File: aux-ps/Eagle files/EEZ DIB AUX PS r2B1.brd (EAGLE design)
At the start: 210 x 60 mm, 117 parts, among them IC1 AMC6821SDBQR, IC2 VIPer35L, IC3 TL431, J1 PF0030/PC, J2 1-726388-2, J3 1-726388-2, J4 1-726388-2, J5 SWEB 8094 AU/GN, Q1 BTA26-600, Q2 BTA26-600, Q3 2N7002, Q4 2N7002, Q5 BSP716NH6327XTSA1, Q6 2N7002, SW1 DF62J12S2AHQA, X1 39-28-1063, X2 39-30-1039, X3 ZL231-16KG, X4 22-23-2031, X5 22-23-2021

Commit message: #30, #31, #32
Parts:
- removed D7: BAS316, EEZ_Lib1:SOD323-R
- removed L4: ECS-MPIL0630-150MC, EEZ_inductors_and_transformers:DE0704
- removed TR1B: (WE 760875532), EEZ_Lib1:WE-UOST
- added C25: 18p, rcl:C0603
- added C26: 33n, rcl:C0805
- added C27: 2n2, rcl:C0805
- added R38: 10K, rcl:R0805
- added R39: 6K8, rcl:R0805
- added R40: 47K, rcl:R0805
- added R41: 4K7, rcl:R0805
- added X6: 22-23-2021, con-molex:22-23-2021
- added ZD4: N.C., EEZ_Lib1:SOD123
- added ZD5: BZT52C20-DC, EEZ_Lib1:SOD123
- C10: value 3n3 -> 1n/1kV; device rcl:C0805 -> rcl:C1210
- C11: value 3n3 -> UCY2G6R8MPD; device rcl:C0805 -> EEZ_Lib1:ECAP5/10.5
- C12: value UVZ1C471MPD -> UCY2G6R8MPD; device EEZ_Lib1:ECAP3.5/8 -> EEZ_Lib1:ECAP5/10.5
- C13: value 4u7 -> 3n3; device rcl:C1210 -> rcl:C0805
- C14: value EEEFK1V470P -> UVZ1C471MPD; device EEZ_Lib1:CAPAE660X610N -> EEZ_Lib1:ECAP3.5/8
- C15: value CY1Y-470P -> 4u7; device EEZ_Lib1:CY075-032X103 -> rcl:C1210
- C16: value 100n -> 3n3; device rcl:C0603 -> rcl:C0805
- C17: value 3n3 -> EEEFK1V470P; device rcl:C0805 -> EEZ_Lib1:CAPAE660X610N
- C18: value 1500u/16V -> CY1Y-470P; device EEZ_Lib1:ECAP5/13 -> EEZ_Lib1:CY075-032X103
- C19: value 4u7 -> 100n; device rcl:C1210 -> rcl:C0603
- C20: value N.C. -> 3n3
- C21: value 33n -> 1500u/16V; device rcl:C0805 -> EEZ_Lib1:ECAP5/13
- C22: value 18p -> 4u7; device rcl:C0603 -> rcl:C1210
- C23: value 33n -> N.C.
- C24: value 2n2 -> 33n
- C4: value 10u -> 1u; device rcl:C1206 -> rcl:C0805
- C5: value UVZ1C471MPD -> 1u; device EEZ_Lib1:ECAP3.5/8 -> rcl:C0805
- C7: value 1n/1kV -> 100n; device rcl:C1210 -> rcl:C0805
- C8, C9: value UCY2G6R8MPD -> 100n; device EEZ_Lib1:ECAP5/10.5 -> rcl:C0603
- D1: value SKL16 -> SS110; device EEZ_Lib1:SOD123 -> EEZ_Lib1:SMB
- D2: value SS110 -> US1K-DIO; device EEZ_Lib1:SMB -> EEZ_Lib1:DO214AA
- D3: value US1K-DIO -> SS110; device EEZ_Lib1:DO214AA -> EEZ_Lib1:SMB
- D4: value SS110 -> SK55
- D5: value SK55 -> BAS316; device EEZ_Lib1:SMB -> EEZ_Lib1:SOD323-R
- IC1: value AMC6821SDBQR -> MAX31760AEE+
- L1: value BLM21PG331SH1 -> RLB0812-471KL; device EEZ_Lib1:0805 -> EEZ_Lib1:FERSYTER_DSZ6
- L2: value RLB0812-471KL -> ECS-MPIL0630-150MC; device EEZ_Lib1:FERSYTER_DSZ6 -> EEZ_inductors_and_transformers:DE0704
- L3: value DLG-0403-180 -> ECS-MPIL0630-150MC; device EEZ_inductors_and_transformers:DE0403 -> EEZ_inductors_and_transformers:DE0704
- Q5: value BSP716NH6327XTSA1 -> 2N7002; device transistor-power:SOT223 -> EEZ_Lib1:SOT103P240X110-3N
- Q6: value 2N7002 -> PSMN0R9-25YLC; device EEZ_Lib1:SOT103P240X110-3N -> EEZ_Lib1:SOT669
- R11: value 2K2 -> 1R
- R12: value 10K -> 470R
- R13: value 470R -> 1K
- R14: value 47K -> 1K
- R15: value 10K -> 4K7
- R16: value 4K7 -> 47K
- R17: value 2K2 -> 10R
- R18: value 220K -> 100R; device rcl:R1206 -> rcl:R0805
- R19: value 220K -> N.C.; device rcl:R1206 -> rcl:R0805
- R20: value 100K -> 10R; device rcl:R1206 -> rcl:R0805
- R21, R22: value 120R -> 100K; device rcl:R0805 -> rcl:R1206
- R23, R28: value 1K -> 100K; device rcl:R0805 -> rcl:R1206
- R24: value 100K -> 120R; device rcl:R1206 -> rcl:R0805
- R25: value 22R -> 100K; device rcl:R0805 -> rcl:R1206
- R26: value 100K -> 1K; device rcl:R1206 -> rcl:R0805
- R27: value 120R -> 22R
- R29: value N.C. -> 120R
- R30: value 4K87 -> 120R
- R31: value 10K -> 1K
- R32: value 47K -> 4K7
- R33: value 10K -> N.C.
- R34: value 6K8 -> 10K
- R35: value 1K8 -> 47K
- R36: value 47K -> 270R
- R37: value 4K7 -> 1K8
- X4: value 22-23-2031 -> 47053-1000; device con-molex:22-23-2031 -> EEZ_connectors:47053-1000
- X5: value 22-23-2021 -> 47053-1000; device con-molex:22-23-2021 -> EEZ_connectors:47053-1000
- ZD3: value BZT52C20-DC -> N.C.
- moved C12 79.4 mm to (134.6, 29.9)
- moved C19 79.0 mm to (129.7, 35.2), turned to 90 degrees
- moved C17 78.2 mm to (135.7, 51.8)
- moved R33 73.3 mm to (135.6, 40.1), turned to 180 degrees
- moved D5 72.0 mm to (136.0, 43.3), turned to 90 degrees
- moved R36 71.3 mm to (51.6, 18.0)
- moved R32 70.7 mm to (51.6, 22.0), turned to 90 degrees
- moved R37 70.2 mm to (129.5, 43.4), turned to 90 degrees
- moved C9 69.2 mm to (51.1, 41.8)
- moved R27 68.7 mm to (125.2, 56.3), turned to 0 degrees
- moved X5 64.1 mm to (103.1, 55.4)
- moved R19 64.1 mm to (45.3, 42.2)
- moved ZD3 63.8 mm to (53.1, 41.5)
- moved C22 62.3 mm to (58.4, 27.1), turned to 0 degrees
- moved R21 61.0 mm to (121.5, 23.0)
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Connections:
- removed net +12V_FAN: C3.1, C5.+, D1.C, L1.1, R12.2, X4.1
- removed net FAN_SENSE: R12.1, R15.2, X4.3
- removed net N$58: IC1.1, Q5.1, R11.2
- new net DRAIN: C7.1, Q6.MB, R11.1
- new net FAN_SENSE1: R13.1, R17.2, X4.3, ZD4.C
- new net FAN_SENSE2: R14.1, R20.2, X5.3, ZD3.C
- new net N$15: C7.2, Q6.4, R18.2
- new net N$17: R21.2, R23.2
- new net N$21: C9.1, IC1.9, R20.1
- new net N$22: R32.1, R36.2
- new net PWM_OUT: IC1.6, R15.2, R18.1, X4.4, X5.4
- net +12V: now also C15.1, C3.1, C5.1, L2.2, X4.2, X5.2; no longer C13.1, L1.2, L3.2
- net +12V_REC: now also C14.+, D1.C, L2.1, R24.1, R26.1; no longer C12.+, D2.C, L3.1, R21.1, R23.1
- net +3V3: now also IC1.16, R13.2, R14.2, R15.1, R19.2; no longer IC1.6, R11.1, R17.2
- net +5V: now also C22.1, L3.2, R16.1, R32.2; no longer C19.1, L4.2, R14.1, R30.2
- net +5V_REC: now also C21.+, D4.C, L3.1, R30.1; no longer C18.+, D5.C, L4.1, R27.1
- net 0V: now also C11.-, C12.-, C17.2, C19.1, C25.2, C27.2, D6.A, R37.2, R39.1, R40.2, ZD5.A; no longer C14.2, C16.1, C22.2, C24.2, C8.-, C9.-, D7.A, R34.1, R35.2, R36.2, TR1B.11, ZD3.A
- net 12VAC: now also C13.2, D1.A; no longer C10.2, D2.A, TR1B.1
- net 5VAC: now also C20.2, D4.A; no longer C17.2, D5.A, TR1B.2, TR1B.3, TR1B.4
- net AUX: now also C16.2, D3.A, D5.A, R33.2; no longer C11.2, D4.A, D6.A, R29.2, TR1B.12
- net AUX_OUT: now also C17.1, C19.2, R27.2, ZD5.C; no longer C14.1, C16.2, R25.2, ZD3.C
- net AUX_REC: now also D3.C, R27.1, R29.1; no longer D4.C, R22.1, R25.1
- net DC_BUS: now also C10.1, C12.+, L1.P$2, R21.1, R22.1; no longer C7.1, C9.+, L2.P$2, R18.1, R19.1, R20.1, TR1B.7
- net FAN_OUT: now also C3.2, C5.2, R11.2, X4.1, X5.1; no longer C5.-, D1.A, Q5.2, Q5.4, X4.2
- net FB1: now also C26.1, R34.2; no longer C23.1, R31.2
- net GND: now also C14.-, C18.2, C21.-, C22.2, C8.2, C9.2, IC1.3, IC1.4, IC1.8, Q5.2, Q6.1, Q6.3, R26.2, R41.1, ZD3.A, ZD4.A; no longer C12.-, C13.2, C18.-, C19.2, C3.2, IC1.11, IC1.12, IC1.13, Q5.3, R16.2, R23.2, R37.1, TR1B.5, TR1B.6
- net N$11: now also R25.2, R28.1; no longer R24.2, R26.1
- net N$12: now also R31.1; no longer R28.1
- net N$13: now also Q5.3, R12.2; no longer Q6.3, R13.2
- net N$137: now also C10.2, D2.C, R23.1; no longer C7.2, D3.C, R18.2, R19.2
- net N$138: now also C24.2, C27.1; no longer C21.2, C24.1
- net N$14: now also R12.1; no longer R13.1
- net N$140: now also C16.1, R29.2; no longer C11.1, R22.2
- net N$141: now also C25.1, R33.1, R35.1, R39.2; no longer C22.1, R29.1, R32.1, R34.2
- net N$146: now also C20.1, R30.2; no longer C17.1, R27.2
- net N$148: now also C23.2, R36.1, R38.2, R41.2; no longer C20.2, R30.1, R33.2, R37.2
- net N$149: now also C23.1, C26.2, R38.1; no longer C20.1, C23.2, R33.1
- net N$152: now also C24.1, R40.1; no longer C21.1, R36.1
- net N$155: now also D5.C, R35.2; no longer D7.C, R32.2
- net N$2: now also C8.1, IC1.7, R17.1; no longer IC1.2, R15.1, R16.1
- net N$20: now also R28.2, R37.1; no longer R26.2, R35.1
- net N$3: now also IC1.12, R19.1; no longer IC1.7, R17.1
- net N$4: now also C18.1; no longer C15.1
- net N$49: now also R22.2, R25.1; no longer R20.2, R24.1
- net N$5: now also R31.2, R34.1; no longer R28.2, R31.1
- net N$8: now also C13.1, R24.2; no longer C10.1, R21.2
- net N$9: now also C11.+, L1.P$1; no longer C8.+, L2.P$1
- net NFAULT: now also IC1.13; no longer IC1.8
- net PWR_DIR_OUT: now also Q5.1, R16.2; no longer Q6.1, R14.2
- net SSCL: now also IC1.15; no longer IC1.16
- net SSDA: now also IC1.14; no longer IC1.15
- net TEMP1_N: now also IC1.2, X6.2; no longer IC1.9, X5.2
- net TEMP1_P: now also IC1.1, X6.1; no longer IC1.10, X5.1
- net VIPER_D: now also D2.A; no longer D3.A, TR1B.9
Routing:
- net GND: track 203.6 -> 90.8 mm, vias 18 -> 20
- net PWM_OUT: track 0.00 -> 89.2 mm, vias 0 -> 3
- net FAN_SENSE2: track 0.00 -> 72.4 mm, vias 0 -> 3
- net FAN_SENSE1: track 0.00 -> 62.4 mm, vias 0 -> 3
- net N$58: track 61.0 -> 0.00 mm, vias 2 -> 0
- net FAN_SENSE: track 56.6 -> 0.00 mm, vias 1 -> 0
- net +3V3: track 43.7 -> 83.7 mm, vias 2 -> 3
- net +12V: track 68.6 -> 107.7 mm
- net +12V_FAN: track 34.7 -> 0.00 mm, vias 1 -> 0
- net N$16: track 73.6 -> 105.9 mm
- net N$14: track 70.0 -> 100.3 mm, vias 0 -> 2
- net PE: track 459.9 -> 489.1 mm
- net PWR_DIR_OUT: track 104.6 -> 132.3 mm, vias 6 -> 5
- net FAN_OUT: track 23.6 -> 45.4 mm
- net 5VAC: track 32.7 -> 11.4 mm
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- added copper zone on layer 1, net DRAIN
- removed copper zone on layer 1, net FAN_OUT
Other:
- board size 210 x 60 mm -> 230.5 x 60 mm
- board text added: "EEZ DIB AUX PS (02/2019 r2B1)"
- board text removed: "EEZ DIB AUX PS (01/2019 r1B2)"

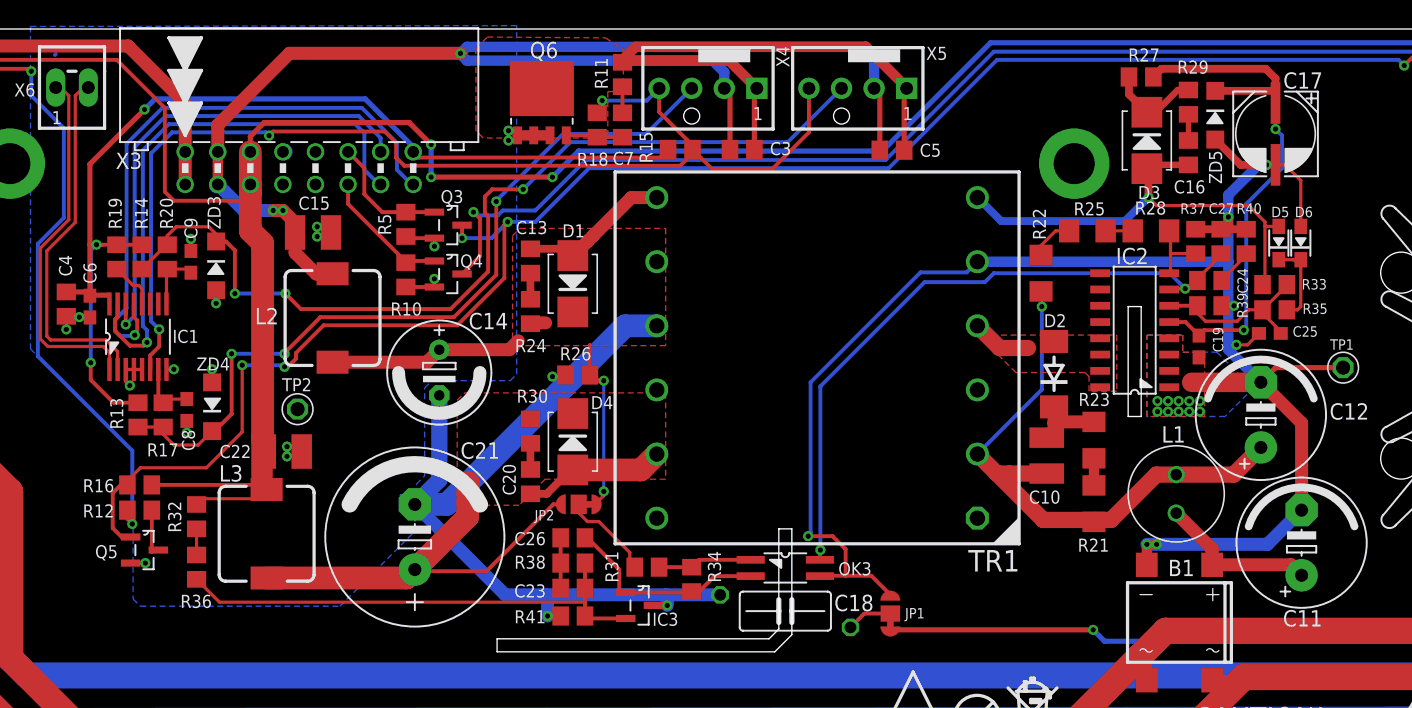
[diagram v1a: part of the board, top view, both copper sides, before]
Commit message: pullup on fan controller SHDN pin, enclosure silkscreens updated
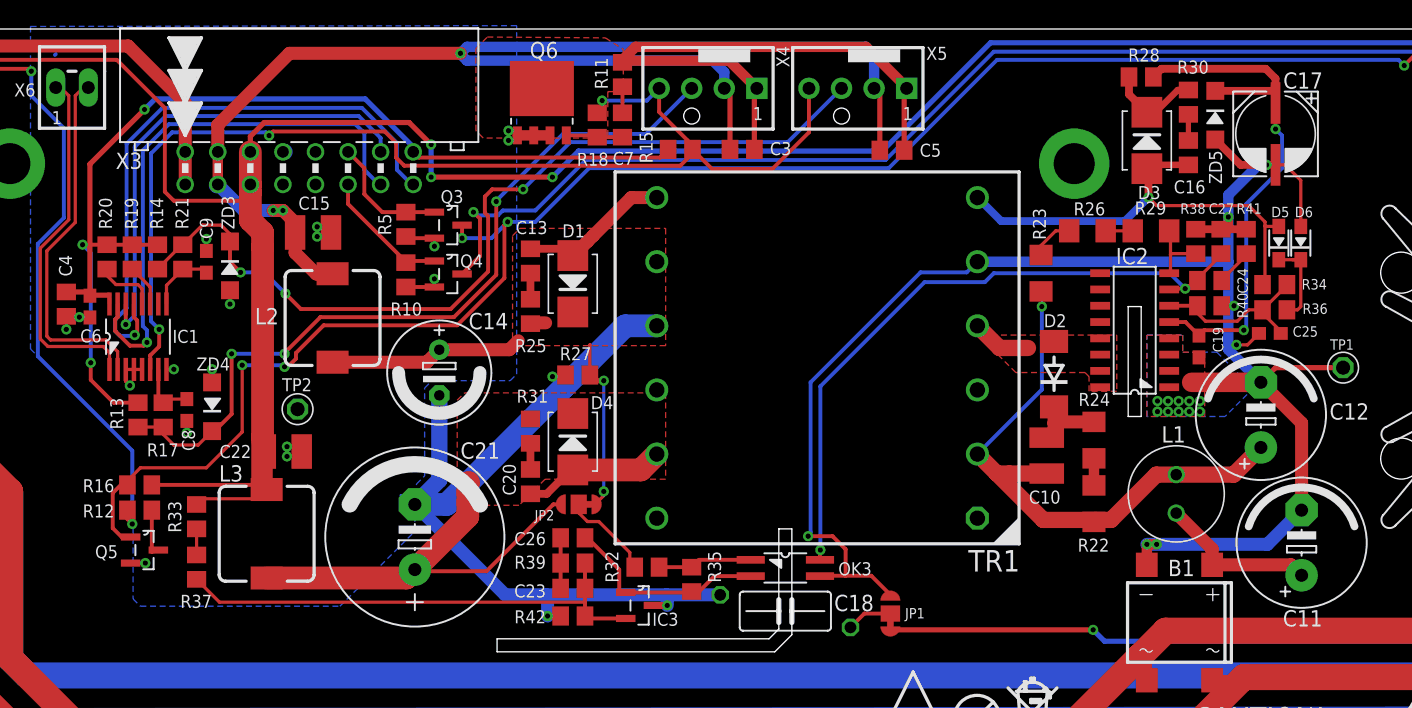
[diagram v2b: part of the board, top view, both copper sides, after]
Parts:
- added R42: 4K7, rcl:R0805
- R19, R33: value N.C. -> 4K7
- R20: value 10R -> N.C.
- R21: value 100K -> 10R; device rcl:R1206 -> rcl:R0805
- R24, R29: value 120R -> 100K; device rcl:R0805 -> rcl:R1206
- R25: value 100K -> 120R; device rcl:R1206 -> rcl:R0805
- R26: value 1K -> 100K; device rcl:R0805 -> rcl:R1206
- R27: value 22R -> 1K
- R28: value 100K -> 22R; device rcl:R1206 -> rcl:R0805
- R31: value 1K -> 120R
- R32: value 4K7 -> 1K
- R34: value 10K -> N.C.
- R35: value 47K -> 10K
- R36: value 270R -> 47K
- R37: value 1K8 -> 270R
- R38: value 10K -> 1K8
- R39: value 6K8 -> 10K
- R40: value 47K -> 6K8
- R41: value 4K7 -> 47K
- moved R36 86.4 mm to (135.6, 38.1), turned to 0 degrees
- moved R33 86.0 mm to (51.6, 22.0), turned to 90 degrees
- moved R37 82.0 mm to (51.6, 18.0)
- moved R21 73.6 mm to (50.5, 42.2)
- moved R41 60.1 mm to (133.4, 43.4), turned to 90 degrees
- moved R30 57.4 mm to (128.9, 54.3)
- moved R38 54.7 mm to (129.5, 43.4), turned to 90 degrees
- moved R39 53.6 mm to (80.9, 18.4), turned to 0 degrees
- moved R34 50.9 mm to (135.6, 40.1), turned to 180 degrees
- moved R35 50.1 mm to (90.2, 17.1), turned to 270 degrees
- moved R27 49.7 mm to (81.3, 33.0), turned to 180 degrees
- moved R24 45.1 mm to (121.5, 27.9), turned to 270 degrees
- moved R25 43.9 mm to (77.6, 38.0), turned to 90 degrees
- moved R26 41.3 mm to (121.0, 44.3), turned to 0 degrees
- moved R32 35.3 mm to (86.7, 18.0), turned to 0 degrees
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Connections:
- new net N$18: IC1.11, R19.1
- net +12V_REC: now also R25.1, R27.1; no longer R24.1, R26.1
- net +3V3: now also R20.2
- net +5V: now also R33.2; no longer R32.2
- net +5V_REC: now also R31.1; no longer R30.1
- net 0V: now also R38.2, R40.1, R41.2; no longer R37.2, R39.1, R40.2
- net AUX: now also R34.2; no longer R33.2
- net AUX_OUT: now also R28.2; no longer R27.2
- net AUX_REC: now also R28.1, R30.1; no longer R27.1, R29.1
- net DC_BUS: now also R23.1; no longer R21.1
- net FAN_SENSE2: now also R21.2; no longer R20.2
- net FB1: now also R35.2; no longer R34.2
- net GND: now also R27.2, R42.1; no longer R26.2, R41.1
- net N$11: now also R26.2, R29.1; no longer R25.2, R28.1
- net N$12: now also R32.1; no longer R31.1
- net N$137: now also R24.1; no longer R23.1
- net N$140: now also R30.2; no longer R29.2
- net N$141: now also R34.1, R36.1, R40.2; no longer R33.1, R35.1, R39.2
- net N$146: now also R31.2; no longer R30.2
- net N$148: now also R37.1, R39.2, R42.2; no longer R36.1, R38.2, R41.2
- net N$149: now also R39.1; no longer R38.1
- net N$152: now also R41.1; no longer R40.1
- net N$155: now also R36.2; no longer R35.2
- net N$17: now also R22.2, R24.2; no longer R21.2, R23.2
- net N$20: now also R29.2, R38.1; no longer R28.2, R37.1
- net N$21: now also R21.1; no longer R20.1
- net N$22: now also R33.1, R37.2; no longer R32.1, R36.2
- net N$3: now also R20.1; no longer R19.1
- net N$49: now also R23.2, R26.1; no longer R22.2, R25.1
- net N$5: now also R32.2, R35.1; no longer R31.2, R34.1
- net N$8: now also R25.2; no longer R24.2
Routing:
- net N$18: track 0.00 -> 3.30 mm
- net FAN_SENSE2: track 72.4 -> 69.6 mm
- net +3V3: track 83.7 -> 86.1 mm
- net N$3: track 3.79 -> 4.86 mm

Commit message: #30
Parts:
- C10: value 1n/1kV -> 2n2/1kV
- R27: value 1K -> 4K7
- R28: value 22R -> 10R
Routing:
- net DC_BUS: track 47.3 -> 48.2 mm
- net VIPER_D: vias 0 -> 4
- added copper zone on layer 16, net VIPER_D
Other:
- outline, holes or cut-outs redrawn
- board text added: "EEZ DIB AUX PS (03/2019 r2B1)"
- board text removed: "EEZ DIB AUX PS (02/2019 r2B1)"

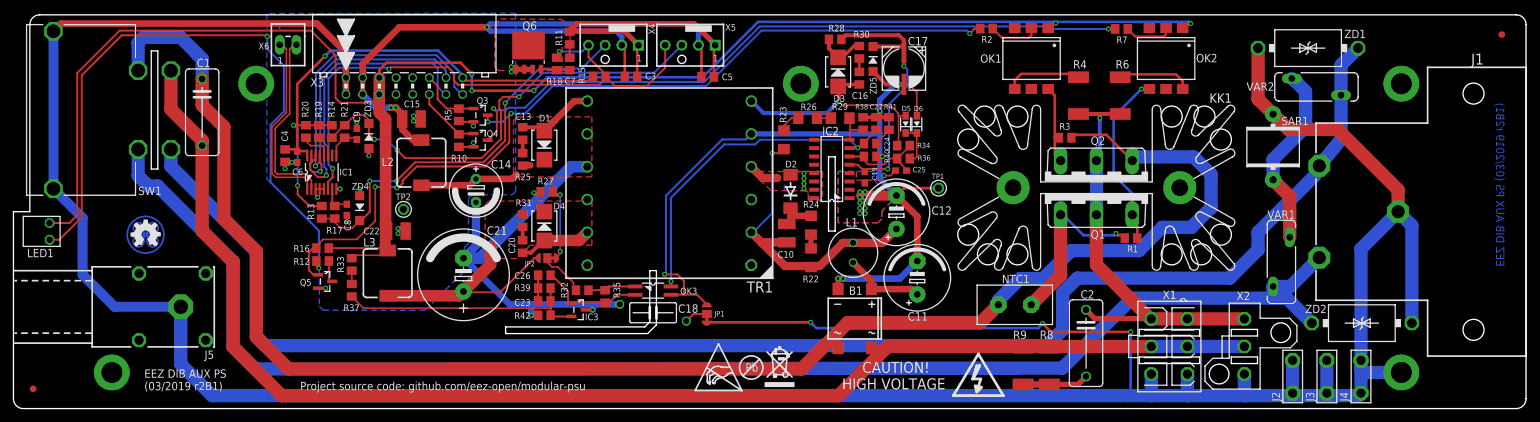
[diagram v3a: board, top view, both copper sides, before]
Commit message: temp. sensor C9 added
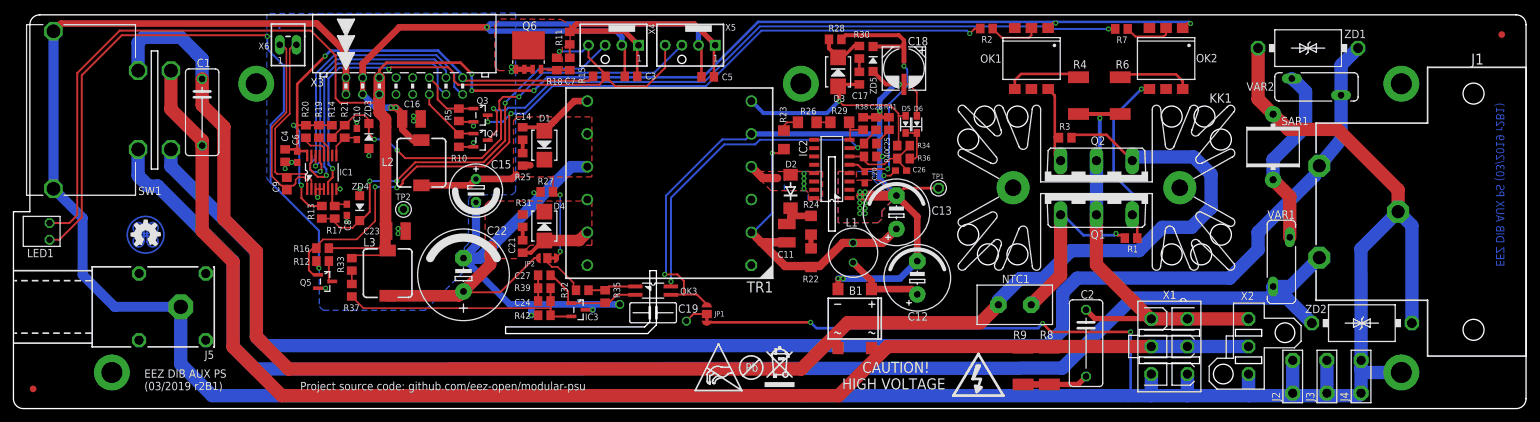
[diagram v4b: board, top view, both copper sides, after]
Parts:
- added C28: 2n2, rcl:C0805
- C10: value 2n2/1kV -> 100n; device rcl:C1210 -> rcl:C0603
- C11: value UCY2G6R8MPD -> 2n2/1kV; device EEZ_Lib1:ECAP5/10.5 -> rcl:C1210
- C13: value 3n3 -> UCY2G6R8MPD; device rcl:C0805 -> EEZ_Lib1:ECAP5/10.5
- C14: value UVZ1C471MPD -> 3n3; device EEZ_Lib1:ECAP3.5/8 -> rcl:C0805
- C15: value 4u7 -> UVZ1C471MPD; device rcl:C1210 -> EEZ_Lib1:ECAP3.5/8
- C16: value 3n3 -> 4u7; device rcl:C0805 -> rcl:C1210
- C17: value EEEFK1V470P -> 3n3; device EEZ_Lib1:CAPAE660X610N -> rcl:C0805
- C18: value CY1Y-470P -> EEEFK1V470P; device EEZ_Lib1:CY075-032X103 -> EEZ_Lib1:CAPAE660X610N
- C19: value 100n -> CY1Y-470P; device rcl:C0603 -> EEZ_Lib1:CY075-032X103
- C20: value 3n3 -> 100n; device rcl:C0805 -> rcl:C0603
- C21: value 1500u/16V -> 3n3; device EEZ_Lib1:ECAP5/13 -> rcl:C0805
- C22: value 4u7 -> 1500u/16V; device rcl:C1210 -> EEZ_Lib1:ECAP5/13
- C23: value N.C. -> 4u7; device rcl:C0805 -> rcl:C1210
- C24: value 33n -> N.C.
- C25: value 18p -> 33n; device rcl:C0603 -> rcl:C0805
- C26: value 33n -> 18p; device rcl:C0805 -> rcl:C0603
- C27: value 2n2 -> 33n
- C9: value 100n -> 2n2; device rcl:C0603 -> rcl:C0805
- R18: value 100R -> 120R
- moved C16 68.5 mm to (60.6, 44.1), turned to 0 degrees
- moved C10 67.3 mm to (52.3, 41.8)
- moved C13 58.2 mm to (134.6, 29.9)
- moved C26 56.6 mm to (135.3, 36.3)
- moved C27 55.6 mm to (80.9, 20.3), turned to 180 degrees
- moved C24 55.2 mm to (80.9, 16.4), turned to 0 degrees
- moved C18 53.3 mm to (135.7, 51.8), turned to 270 degrees
- moved C20 53.2 mm to (129.7, 35.2), turned to 90 degrees
- moved C19 38.3 mm to (97.5, 14.6), turned to 180 degrees
- moved C23 24.9 mm to (58.4, 27.1)
- moved C11 21.0 mm to (117.9, 26.7)
- moved C15 14.7 mm to (70.5, 33.2), turned to 270 degrees
- moved C9 13.1 mm to (41.7, 34.2)
- moved C22 12.2 mm to (68.6, 20.4), turned to 90 degrees
- moved C14 11.2 mm to (77.6, 41.9), turned to 90 degrees
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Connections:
- net +12V: now also C16.1; no longer C15.1
- net +12V_REC: now also C15.+; no longer C14.+
- net +5V: now also C23.1; no longer C22.1
- net +5V_REC: now also C22.+; no longer C21.+
- net 0V: now also C13.-, C18.2, C20.1, C26.2, C28.2; no longer C11.-, C17.2, C19.1, C25.2, C27.2
- net 12VAC: now also C14.2; no longer C13.2
- net 5VAC: now also C21.2; no longer C20.2
- net AUX: now also C17.2; no longer C16.2
- net AUX_OUT: now also C18.1, C20.2; no longer C17.1, C19.2
- net DC_BUS: now also C11.1, C13.+; no longer C10.1, C12.+
- net FB1: now also C27.1; no longer C26.1
- net GND: now also C10.2, C15.-, C16.2, C19.2, C22.-, C23.2; no longer C14.-, C15.2, C18.2, C21.-, C22.2, C9.2
- net N$137: now also C11.2; no longer C10.2
- net N$138: now also C25.2, C28.1; no longer C24.2, C27.1
- net N$140: now also C17.1; no longer C16.1
- net N$141: now also C26.1; no longer C25.1
- net N$146: now also C21.1; no longer C20.1
- net N$148: now also C24.2; no longer C23.2
- net N$149: now also C24.1, C27.2; no longer C23.1, C26.2
- net N$152: now also C25.1; no longer C24.1
- net N$21: now also C10.1; no longer C9.1
- net N$4: now also C19.1; no longer C18.1
- net N$8: now also C14.1; no longer C13.1
- net N$9: now also C12.+; no longer C11.+
- net TEMP1_N: now also C9.2
- net TEMP1_P: now also C9.1
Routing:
- net TEMP1_P: track 28.3 -> 31.1 mm
- net +3V3: track 86.1 -> 87.0 mm
- net AC_OUT_L: track 66.2 -> 66.8 mm
- net AC_N_OUT: track 209.3 -> 209.9 mm
- net TEMP1_N: track 28.4 -> 29.0 mm
